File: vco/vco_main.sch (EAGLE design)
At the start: 101 parts, among them IC1 OPA4130U, IC2 LM13700M, IC3 OPA4130U, IC4 OPA4130U, Q1 MMBFJ3

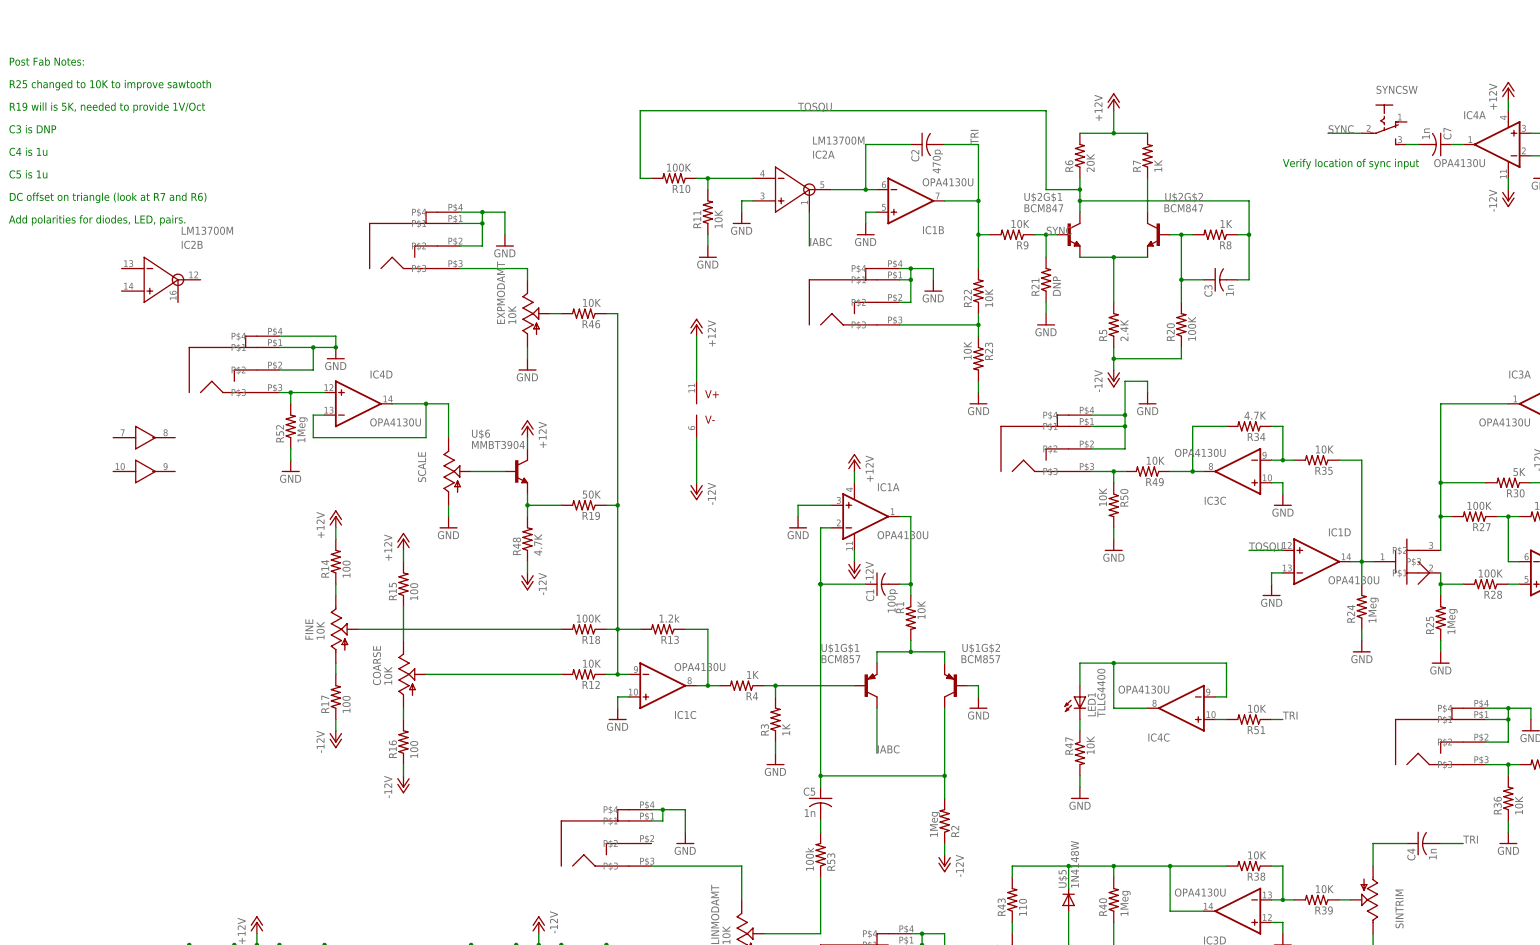
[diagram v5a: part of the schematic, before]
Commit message: fixed most of the silkscreen issues.
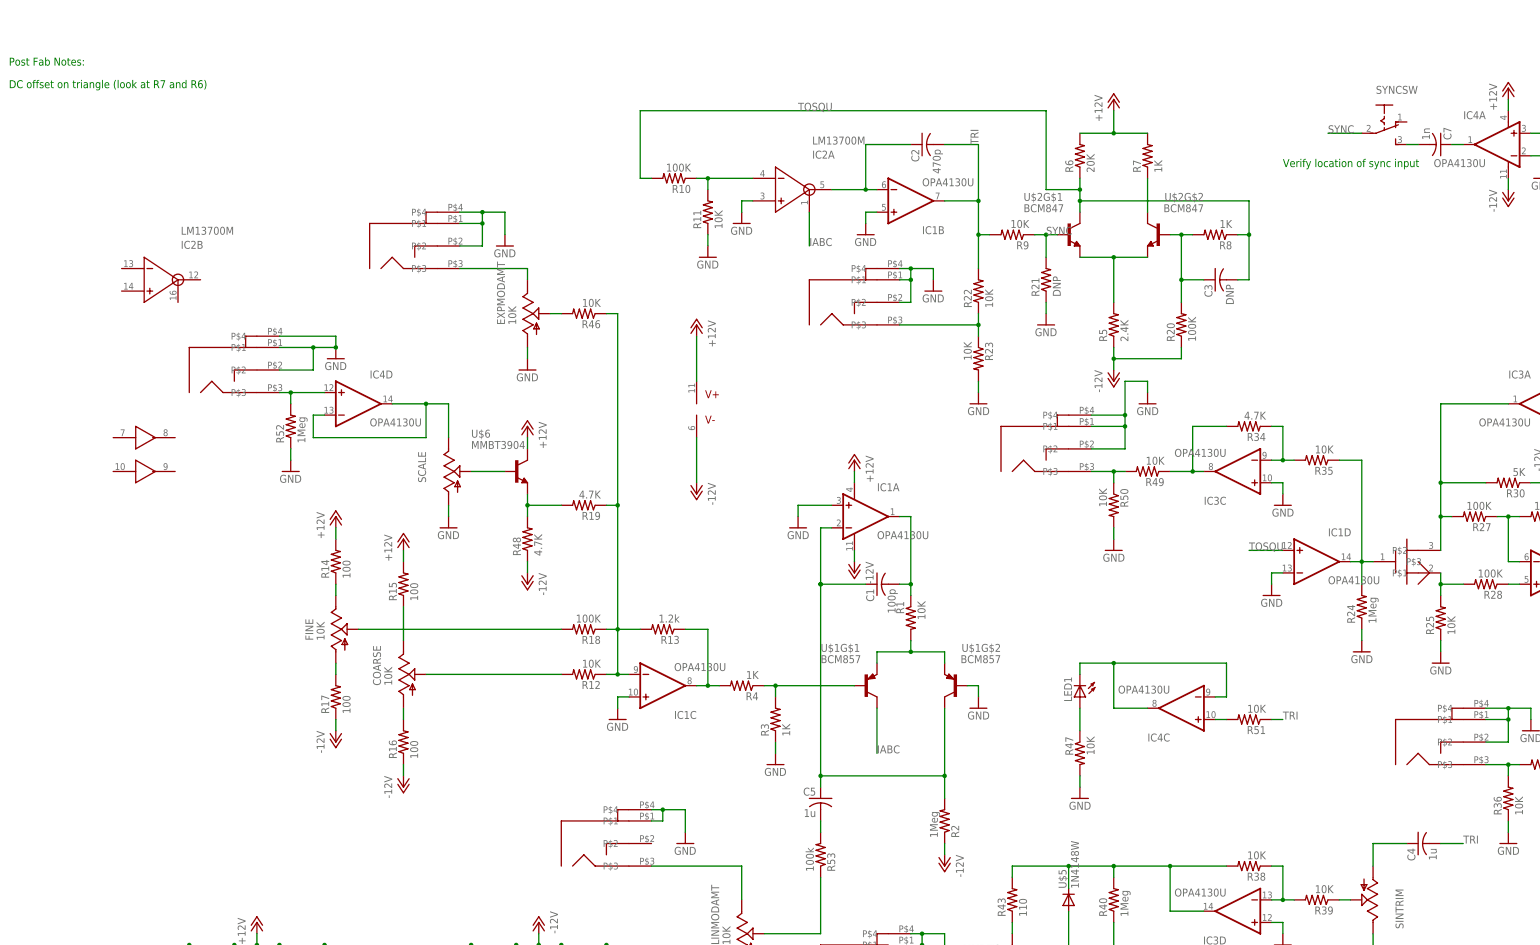
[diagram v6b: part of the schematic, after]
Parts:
- C3: value 1n -> DNP
- C4, C5: value 1n -> 1u
- LED1: value TLLG4400 -> (none); device dan:TLLG4400 -> dan:LED5MM
- R19: value 50K -> 4.7K
- R25: value 1Meg -> 10K
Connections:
- removed net N$53: LED1.C, R47.1
- new net N$1: LED1.A, R47.1
- net N$52: now also LED1.C; no longer LED1.A
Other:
- note removed: "Add polarities for diodes, LED, pairs."
- note removed: "C3 is DNP"
- note removed: "C4 is 1u"
- note removed: "C5 is 1u"
- note removed: "R19 will is 5K, needed to provide 1V/Oct"
- note removed: "R25 changed to 10K to improve sawtooth"
- moved on the sheet: LED1
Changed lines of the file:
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@@
 <part name="P+2" library="dan" deviceset="+12V" device=""/>
 <part name="R18" library="dan" deviceset="R-US_" device="R0603" value="100K"/>
-<part name="R19" library="dan" deviceset="R-US_" device="R0603" value="50K"/>
+<part name="R19" library="dan" deviceset="R-US_" device="R0603" value="4.7K"/>
 <part name="P-5" library="dan" deviceset="-12V" device=""/>
 <part name="SCALE" library="dan" deviceset="TRIM_US-" device="B64Y"/>
@@
 <part name="C2" library="dan" deviceset="C-US" device="C0603" value="470p"/>
 <part name="R20" library="dan" deviceset="R-US_" device="R0603" value="100K"/>
-<part name="C3" library="dan" deviceset="C-US" device="C0603" value="1n"/>
+<part name="C3" library="dan" deviceset="C-US" device="C0603" value="DNP"/>
 <part name="R21" library="dan" deviceset="R-US_" device="R0603" value="DNP"/>
 <part name="GND10" library="dan" deviceset="GND" device=""/>
@@
 <part name="R24" library="dan" deviceset="R-US_" device="R0603" value="1Meg"/>
 <part name="GND14" library="dan" deviceset="GND" device=""/>
-<part name="R25" library="dan" deviceset="R-US_" device="R0603" value="1Meg"/>
+<part name="R25" library="dan" deviceset="R-US_" device="R0603" value="10K"/>
 <part name="GND15" library="dan" deviceset="GND" device=""/>
 <part name="IC3" library="dan" deviceset="OPA4130" device="U"/>
@@
 <part name="GND19" library="dan" deviceset="GND" device=""/>
 <part name="GND20" library="dan" deviceset="GND" device=""/>
-<part name="C4" library="dan" deviceset="C-US" device="C0603" value="1n"/>
+<part name="C4" library="dan" deviceset="C-US" device="C0603" value="1u"/>
 <part name="SINTRIM" library="dan" deviceset="TRIM_US-" device="B64Y"/>
 <part name="R38" library="dan" deviceset="R-US_" device="R0603" value="10K"/>
@@
 <part name="EXPMOD" library="dan" deviceset="PJ301BM" device=""/>
 <part name="GND27" library="dan" deviceset="GND" device=""/>
-<part name="C5" library="dan" deviceset="C-US" device="C0603" value="1n"/>
+<part name="C5" library="dan" deviceset="C-US" device="C0603" value="1u"/>
 <part name="LINMOD" library="dan" deviceset="PJ301BM" device=""/>
 <part name="GND28" library="dan" deviceset="GND" device=""/>
@@
 <part name="GND31" library="dan" deviceset="GND" device=""/>
 <part name="SYNCSW" library="dan" deviceset="255SB" device=""/>
-<part name="LED1" library="dan" deviceset="TLLG4400" device=""/>
 <part name="R47" library="dan" deviceset="R-US_" device="R0603" value="10K"/>
 <part name="GND32" library="dan" deviceset="GND" device=""/>
@@
 <part name="GND38" library="dan" deviceset="GND" device=""/>
 <part name="R53" library="dan" deviceset="R-US_" device="R0603" value="100k"/>
+<part name="LED1" library="dan" deviceset="LED" device="5MM"/>
 </parts>
 <sheets>
@@
 <text x="165.1" y="132.08" size="1.778" layer="91">Verify location of sync input</text>
 <text x="-121.92" y="154.94" size="1.778" layer="91">Post Fab Notes:</text>
-<text x="-121.92" y="149.86" size="1.778" layer="91">R25 changed to 10K to improve sawtooth</text>
-<text x="-121.92" y="144.78" size="1.778" layer="91">R19 will is 5K, needed to provide 1V/Oct</text>
-<text x="-121.92" y="124.46" size="1.778" layer="91">DC offset on triangle (look at R7 and R6)</text>
-<text x="-121.92" y="139.7" size="1.778" layer="91">C3 is DNP</text>
-<text x="-121.92" y="134.62" size="1.778" layer="91">C4 is 1u</text>
-<text x="-121.92" y="129.54" size="1.778" layer="91">C5 is 1u</text>
-<text x="-121.92" y="119.38" size="1.778" layer="91">Add polarities for diodes, LED, pairs.</text>
+<text x="-121.92" y="149.86" size="1.778" layer="91">DC offset on triangle (look at R7 and R6)</text>
 </plain>
 <instances>
@@
 <instance part="GND31" gate="1" x="259.08" y="132.08" rot="MR0"/>
 <instance part="SYNCSW" gate="1" x="187.96" y="142.24" rot="R270"/>
-<instance part="LED1" gate="G$1" x="119.38" y="12.7"/>
 <instance part="R47" gate="G$1" x="119.38" y="0" rot="MR270"/>
 <instance part="GND32" gate="1" x="119.38" y="-10.16" rot="MR0"/>
@@
 <instance part="GND38" gate="1" x="43.18" y="-53.34"/>
 <instance part="R53" gate="G$1" x="60.96" y="-22.86" rot="MR90"/>
+<instance part="LED1" gate="G$1" x="119.38" y="12.7" rot="R180"/>
 </instances>
 <busses>
@@
 <wire x1="127" y1="10.16" x2="134.62" y2="10.16" width="0.1524" layer="91"/>
 <wire x1="127" y1="20.32" x2="119.38" y2="20.32" width="0.1524" layer="91"/>
-<pinref part="LED1" gate="G$1" pin="A"/>
-<wire x1="119.38" y1="20.32" x2="119.38" y2="15.24" width="0.1524" layer="91"/>
 <junction x="127" y="20.32"/>
-</segment>
-</net>
-<net name="N$53" class="0">
-<segment>
-<pinref part="R47" gate="G$1" pin="1"/>
 <pinref part="LED1" gate="G$1" pin="C"/>
-<wire x1="119.38" y1="5.08" x2="119.38" y2="7.62" width="0.1524" layer="91"/>
+<wire x1="119.38" y1="17.78" x2="119.38" y2="20.32" width="0.1524" layer="91"/>
 </segment>
 </net>
@@
 </segment>
 </net>
+<net name="N$1" class="0">
+<segment>
+<pinref part="LED1" gate="G$1" pin="A"/>
+<pinref part="R47" gate="G$1" pin="1"/>
+<wire x1="119.38" y1="10.16" x2="119.38" y2="5.08" width="0.1524" layer="91"/>
+</segment>
+</net>
